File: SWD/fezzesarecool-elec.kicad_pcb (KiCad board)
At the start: 2 copper layers, 18 parts, among them J1 Conn_01x10, J10 SWD-6, J11 SWD-7, J12 SWD-8, J5 SWD-1, J6 SWD-2, J7 SWD-3, J8 SWD-4, J9 SWD-5, U10 SN74LVC1G00, U3 SN74CB3Q3257, U4 SN74CB3Q3257, U8 SN74CB3Q3257, U9 SN74CB3Q3257

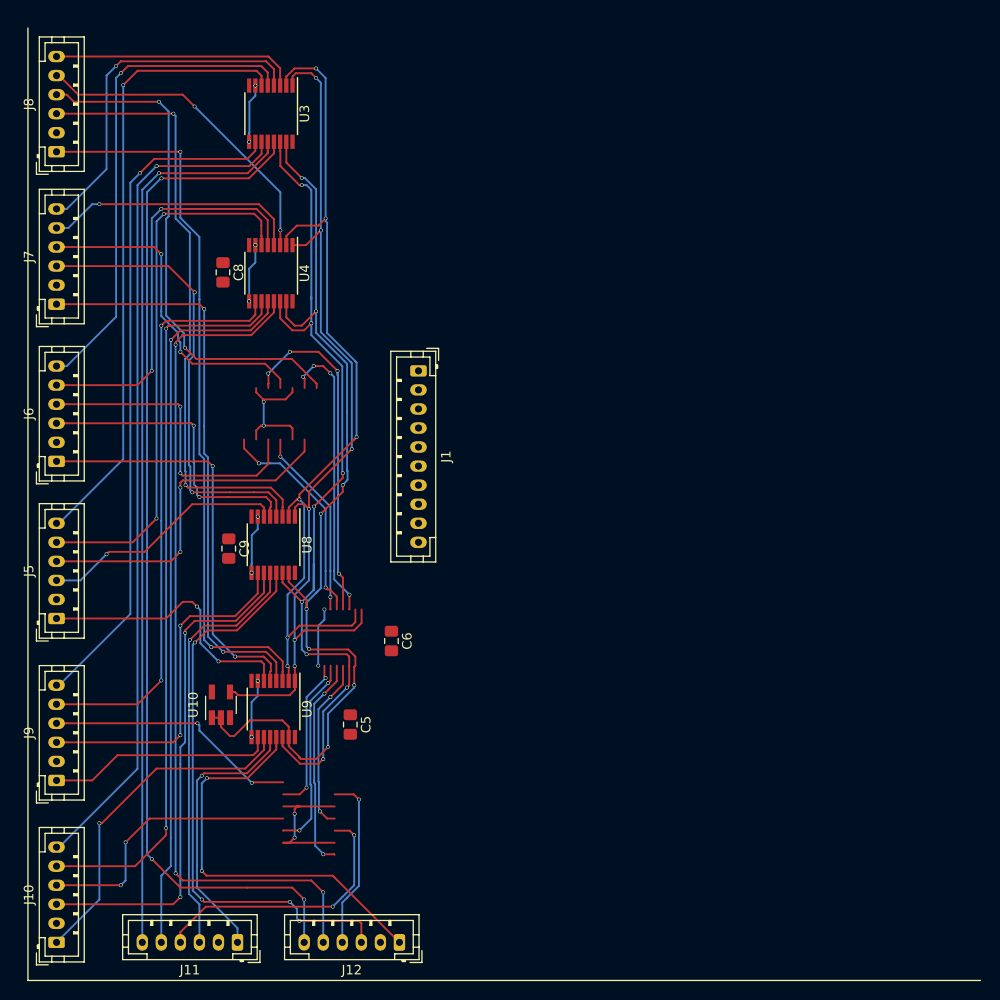
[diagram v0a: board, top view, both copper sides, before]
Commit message: multiplexeur routed
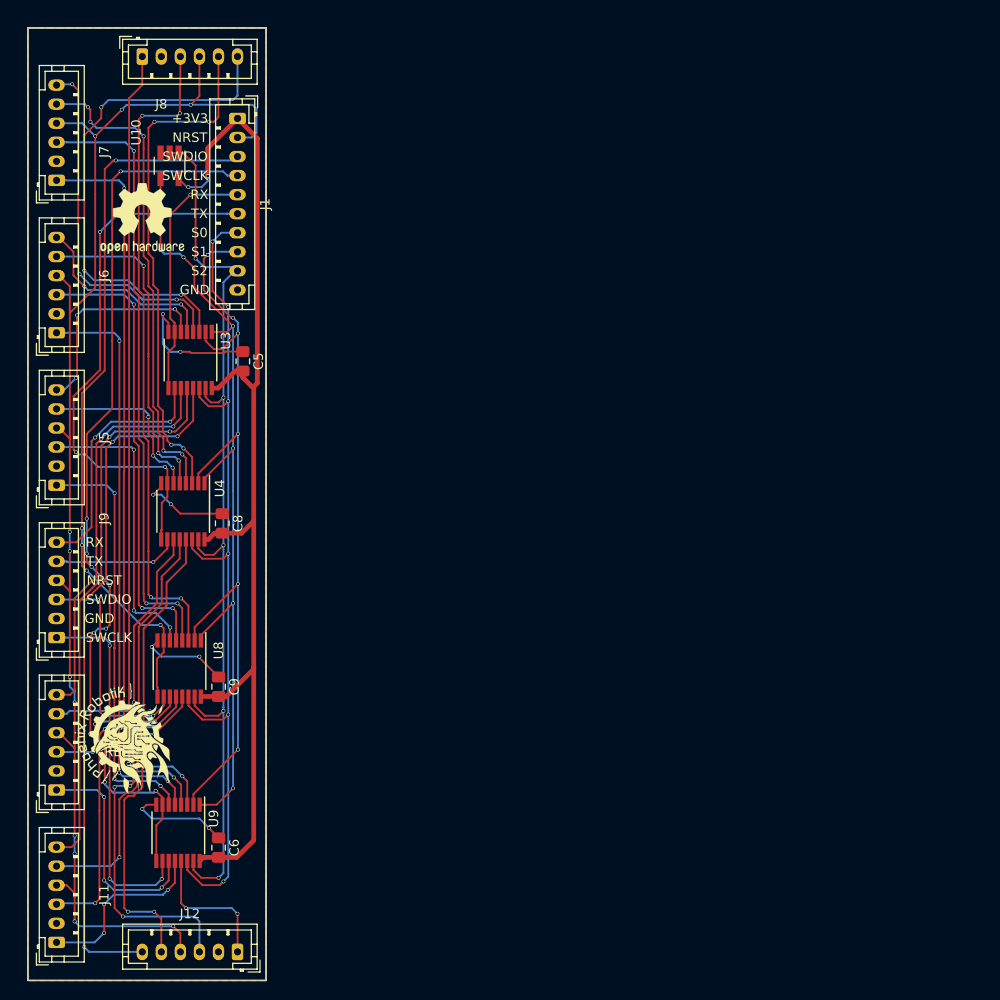
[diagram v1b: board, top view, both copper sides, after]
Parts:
- added REF**: OSHW-Logo2_9.8x8mm_SilkScreen, Symbol:OSHW-Logo2_9.8x8mm_SilkScreen, F.Cu at (177.0, 111.0)
- added REF**: KiCad-Logo2_12mm_SilkScreen, Symbol:KiCad-Logo2_12mm_SilkScreen, B.Cu at (177.0, 140.0)
- added REF**: Logo_14,5mm, PhoenixRobotik:Logo_14,5mm, F.Cu at (175.0, 167.0)
- moved U10 56.8 mm to (179.9, 105.5), turned to 270 degrees
- moved C5 39.8 mm to (187.6, 126.0)
- moved J1 32.6 mm to (187.0, 100.5)
- moved C6 28.3 mm to (185.0, 177.1)
- moved U3 27.2 mm to (182.0, 125.9)
- moved U4 26.7 mm to (181.3, 141.8)
- moved C8 26.4 mm to (185.4, 143.0)
- moved J11 19.0 mm to (168.0, 187.0), turned to 90 degrees
- moved J12 17.0 mm to (187.0, 188.0)
- moved U9 16.4 mm to (180.7, 175.5)
- moved U8 16.3 mm to (180.9, 158.2)
- moved J10 16.0 mm to (168.0, 171.0)
- moved J9 15.0 mm to (168.0, 155.0)
- moved C9 14.5 mm to (185.0, 160.2)
- moved J5 14.0 mm to (168.0, 139.0)
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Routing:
- net +3V3: track 0.00 -> 113.9 mm, vias 0 -> 2
- net /SWD/SWCLK: track 6.17 -> 95.4 mm, vias 2 -> 11
- net /SWD/nrst: track 224.3 -> 144.2 mm, vias 15 -> 11
- net /SWD/SWDIO: track 6.17 -> 75.9 mm, vias 2 -> 5
- net /SWD/TX: track 6.17 -> 57.8 mm, vias 2 -> 3
- net Net-(J10-Pad5): track 78.1 -> 27.7 mm, vias 2 -> 1
- net Net-(J9-Pad5): track 61.1 -> 13.2 mm, vias 2 -> 1
- net Net-(J10-Pad6): track 88.8 -> 42.1 mm, vias 1 -> 2
- net Net-(J9-Pad6): track 71.6 -> 26.2 mm, vias 1 -> 2
- net GND: track 0.00 -> 44.1 mm, vias 0 -> 8
- net Net-(J5-Pad6): track 65.7 -> 22.4 mm, vias 1 -> 3
- net Net-(J8-Pad4): track 43.0 -> 0.00 mm, vias 2 -> 0
- net Net-(J12-Pad5): track 90.1 -> 49.7 mm, vias 3 -> 2
- net Net-(J5-Pad5): track 57.5 -> 18.7 mm, vias 2 -> 3
- net Net-(J10-Pad3): track 53.5 -> 16.5 mm, vias 2 -> 3
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- added copper zone on B.Cu, net GND
- added copper zone on F.Cu, net GND
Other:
- board outline added: 25 x 100 mm
- board text added: "+3V3"
- board text added: "GND"
- board text added: "NRST"
- board text added: "RX"
- board text added: "S0"
- board text added: "S1"
- board text added: "S2"
- board text added: "SWCLK"
- board text added: "SWDIO"
- board text added: "TX"

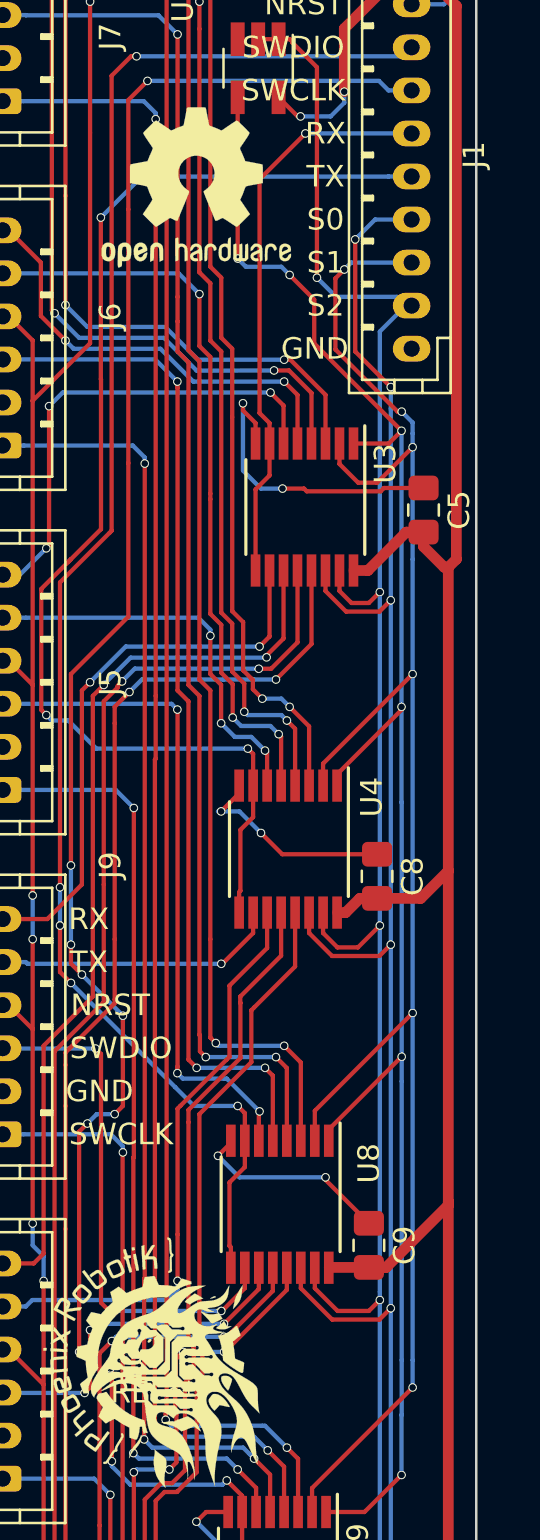
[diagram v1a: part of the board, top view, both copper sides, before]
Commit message: holes addes
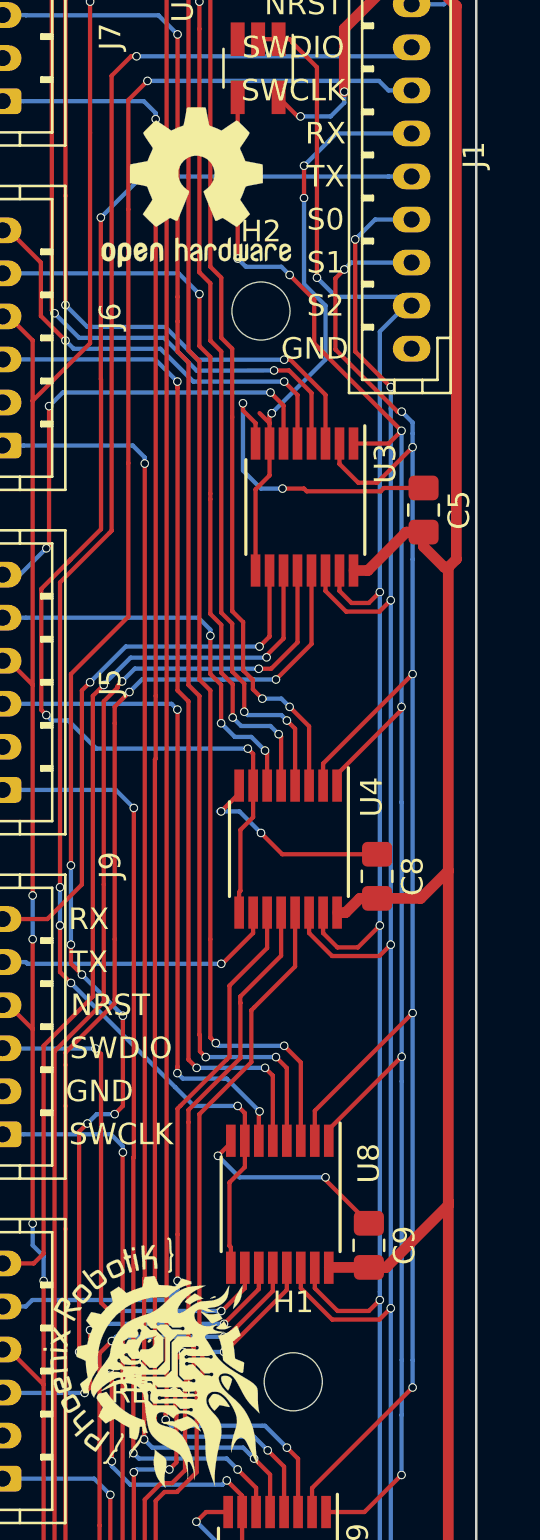
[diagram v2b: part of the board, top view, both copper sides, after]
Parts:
- added H1: MountingHole, MountingHole:MountingHole_2.7mm_M2.5, F.Cu at (181.5, 166.5)
- added H2: MountingHole, MountingHole:MountingHole_2.7mm_M2.5, F.Cu at (180.0, 116.8)
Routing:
- net /SWD/RX: track 26.6 -> 26.8 mm, vias 1 -> 3

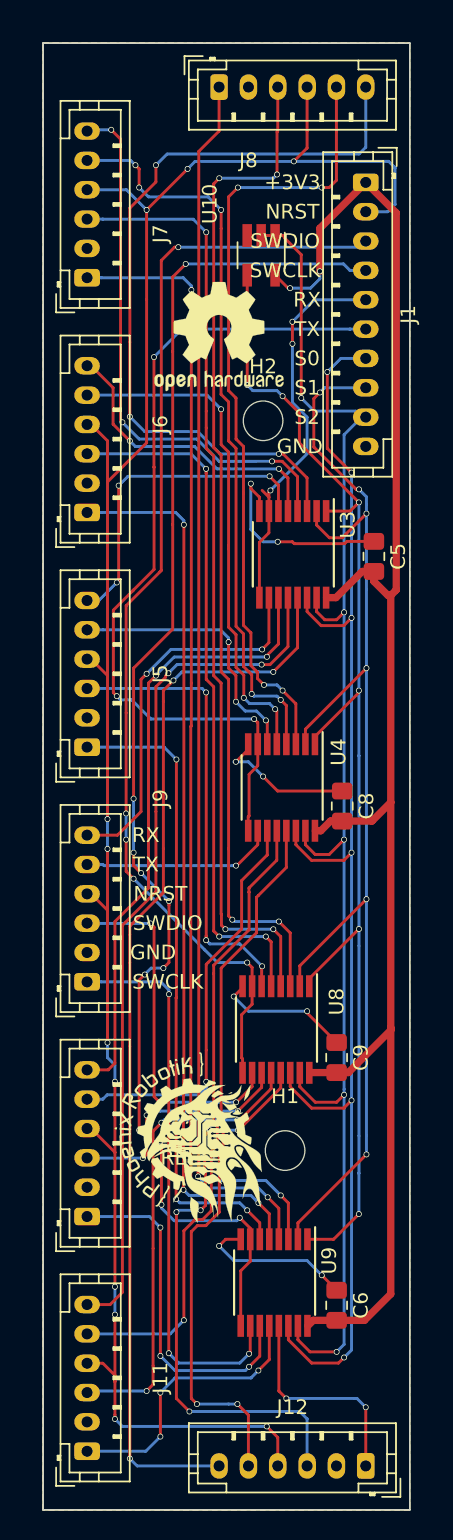
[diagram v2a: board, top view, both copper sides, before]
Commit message: connectors reorganised
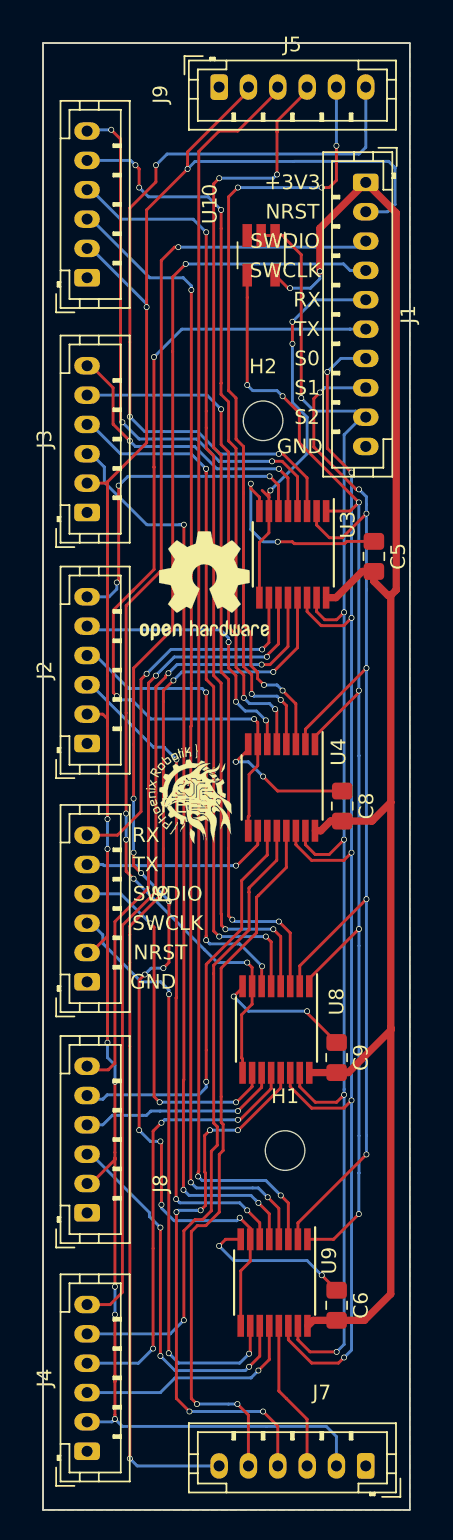
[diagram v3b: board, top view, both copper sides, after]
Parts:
- removed J10: SWD-6, Connector_JST:JST_PH_B6B-PH-K_1x06_P2.00mm_Vertical
- removed J11: SWD-7, Connector_JST:JST_PH_B6B-PH-K_1x06_P2.00mm_Vertical
- removed J12: SWD-8, Connector_JST:JST_PH_B6B-PH-K_1x06_P2.00mm_Vertical
- removed the REF** at (177.0, 140.0)
- removed the REF** at (175.0, 167.0)
- added J2: Conn_Debug, Connector_JST:JST_PH_B6B-PH-K_1x06_P2.00mm_Vertical, F.Cu at (168.0, 138.8)
- added J3: Conn_Debug, Connector_JST:JST_PH_B6B-PH-K_1x06_P2.00mm_Vertical, F.Cu at (168.0, 123.0)
- added J4: Conn_Debug, Connector_JST:JST_PH_B6B-PH-K_1x06_P2.00mm_Vertical, F.Cu at (168.0, 187.0)
- added REF**: KiCad-Logo2_8mm_SilkScreen, Symbol:KiCad-Logo2_8mm_SilkScreen, B.Cu at (178.0, 143.0)
- added REF**: Logo_8,5mm, PhoenixRobotik:Logo_8,5mm, F.Cu at (175.0, 143.0)
- J5: value SWD-1 -> Conn_Debug
- J6: value SWD-2 -> Conn_Debug
- J7: value SWD-3 -> Conn_Debug
- J8: value SWD-4 -> Conn_Debug
- J9: value SWD-5 -> Conn_Debug
- moved J7 83.2 mm to (187.0, 188.0), turned to 180 degrees
- moved J8 77.3 mm to (168.0, 170.8), turned to 90 degrees
- moved J9 48.0 mm to (168.0, 107.0)
- moved J5 45.9 mm to (177.0, 94.0), turned to 0 degrees
- moved J6 32.0 mm to (168.0, 155.0)
- moved REF** 17.0 mm to (176.0, 128.0)
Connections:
- J5 pad 1: Net-(J5-Pad1) -> GND
- J5 pad 2: GND -> /SWD/nrst
- J5 pad 4: /SWD/nrst -> Net-(J5-Pad4)
- J6 pad 1: Net-(J6-Pad1) -> GND
- J6 pad 2: GND -> /SWD/nrst
- J6 pad 4: /SWD/nrst -> Net-(J6-Pad4)
- J7 pad 1: Net-(J7-Pad1) -> GND
- J7 pad 2: GND -> /SWD/nrst
- J7 pad 4: /SWD/nrst -> Net-(J7-Pad4)
- J8 pad 1: Net-(J8-Pad1) -> GND
- J8 pad 2: GND -> /SWD/nrst
- J8 pad 4: /SWD/nrst -> Net-(J8-Pad4)
- J9 pad 1: Net-(J9-Pad1) -> GND
- J9 pad 2: GND -> /SWD/nrst
- J9 pad 4: /SWD/nrst -> Net-(J9-Pad4)
- U3 pad 10: Net-(J9-Pad6) -> Net-(J6-Pad6)
- U3 pad 11: Net-(J10-Pad6) -> Net-(J8-Pad6)
- U3 pad 13: Net-(J12-Pad6) -> Net-(J7-Pad6)
- U3 pad 3: Net-(J8-Pad6) -> Net-(J5-Pad6)
- U3 pad 4: Net-(J7-Pad6) -> Net-(J9-Pad6)
- U3 pad 5: Net-(J6-Pad6) -> Net-(J3-Pad6)
- U3 pad 6: Net-(J5-Pad6) -> Net-(J2-Pad6)
- U4 pad 10: Net-(J9-Pad5) -> Net-(J6-Pad5)
- U4 pad 11: Net-(J10-Pad5) -> Net-(J8-Pad5)
- U4 pad 13: Net-(J12-Pad5) -> Net-(J7-Pad5)
- U4 pad 3: Net-(J8-Pad5) -> Net-(J5-Pad5)
- U4 pad 4: Net-(J7-Pad5) -> Net-(J9-Pad5)
- U4 pad 5: Net-(J6-Pad5) -> Net-(J3-Pad5)
- U4 pad 6: Net-(J5-Pad5) -> Net-(J2-Pad5)
- U8 pad 10: Net-(J9-Pad3) -> Net-(J6-Pad4)
- U8 pad 11: Net-(J10-Pad3) -> Net-(J8-Pad4)
- U8 pad 13: Net-(J12-Pad3) -> Net-(J7-Pad4)
- U8 pad 3: Net-(J8-Pad3) -> Net-(J5-Pad4)
- U8 pad 4: Net-(J7-Pad3) -> Net-(J9-Pad4)
- U8 pad 5: Net-(J6-Pad3) -> Net-(J3-Pad4)
- U8 pad 6: Net-(J5-Pad3) -> Net-(J2-Pad4)
- U9 pad 10: Net-(J9-Pad1) -> Net-(J6-Pad3)
- U9 pad 11: Net-(J10-Pad1) -> Net-(J8-Pad3)
- U9 pad 13: Net-(J12-Pad1) -> Net-(J7-Pad3)
- U9 pad 3: Net-(J8-Pad1) -> Net-(J5-Pad3)
- U9 pad 4: Net-(J7-Pad1) -> Net-(J9-Pad3)
- U9 pad 5: Net-(J6-Pad1) -> Net-(J3-Pad3)
- U9 pad 6: Net-(J5-Pad1) -> Net-(J2-Pad3)
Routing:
- net Net-(J8-Pad1): track 84.2 -> 0.00 mm, vias 2 -> 0
- net Net-(J7-Pad1): track 77.3 -> 0.00 mm, vias 3 -> 0
- net Net-(J12-Pad6): track 73.5 -> 0.00 mm, vias 3 -> 0
- net Net-(J5-Pad4): track 0.00 -> 70.1 mm, vias 0 -> 4
- net Net-(J9-Pad4): track 0.00 -> 64.7 mm, vias 0 -> 3
- net Net-(J3-Pad3): track 0.00 -> 62.8 mm, vias 0 -> 3
- net Net-(J6-Pad1): track 60.7 -> 0.00 mm, vias 3 -> 0
- net Net-(J5-Pad3): track 31.1 -> 86.6 mm, vias 3 -> 2
- net Net-(J9-Pad3): track 24.5 -> 79.0 mm
- net Net-(J7-Pad3): track 63.9 -> 10.5 mm, vias 3 -> 0
- net Net-(J12-Pad5): track 49.7 -> 0.00 mm, vias 2 -> 0
- net Net-(J3-Pad4): track 0.00 -> 48.6 mm, vias 0 -> 3
- net Net-(J2-Pad3): track 0.00 -> 45.7 mm, vias 0 -> 3
- net Net-(J5-Pad1): track 43.9 -> 0.00 mm, vias 3 -> 0
- net Net-(J8-Pad3): track 69.2 -> 25.7 mm, vias 4 -> 3
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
